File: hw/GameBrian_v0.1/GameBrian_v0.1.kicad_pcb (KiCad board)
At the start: 6 copper layers, 136.4 x 144.3 mm, 121 parts, among them J1 USB_C_Receptacle_USB2.0_16P, J2 GameBoy_GamePak_AGB-002, J3 Micro_SD_Card_Det_Hirose_DM3AT, J4 Debug, J5 Config, J6 GPIO, Q1 Q_NMOS_GSD, Q2 Q_NMOS_GSD, SW10 Program, SW8 Reset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

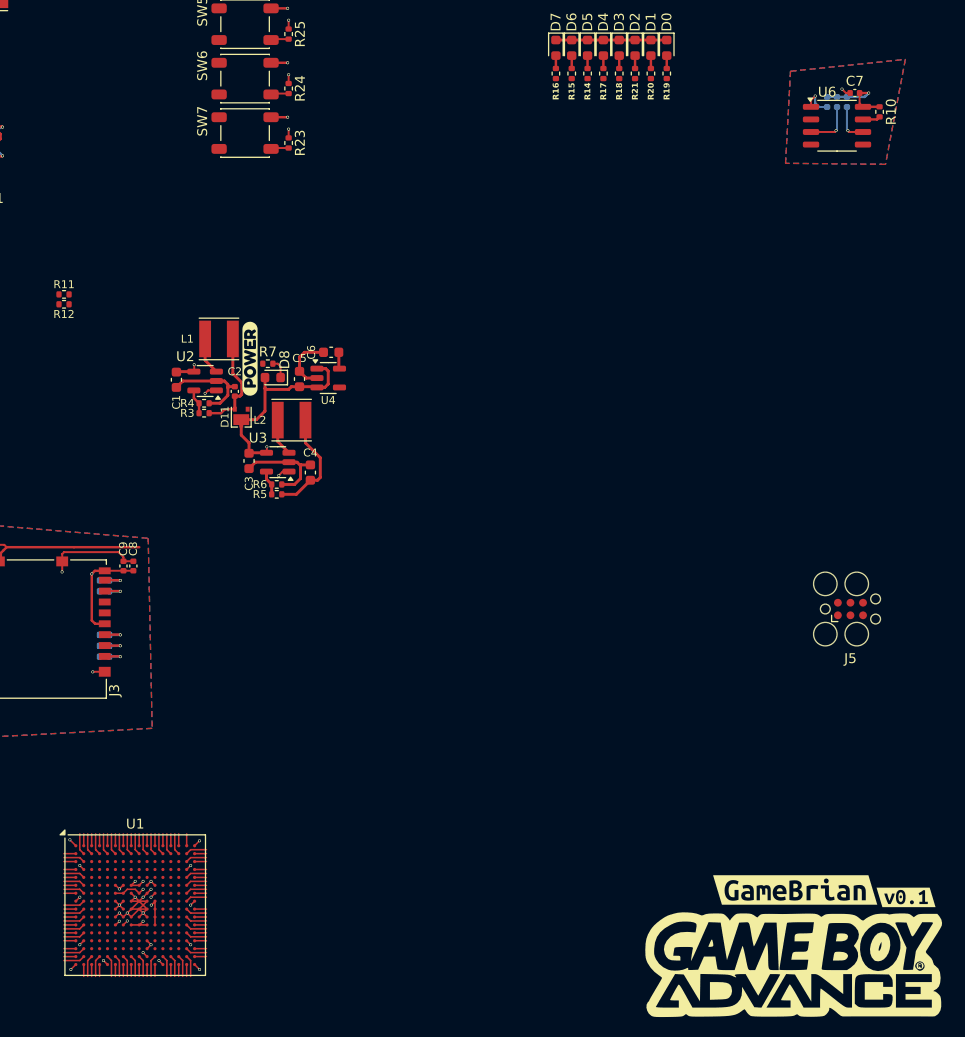
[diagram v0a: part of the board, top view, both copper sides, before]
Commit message: Checkpoint (pre-final route)
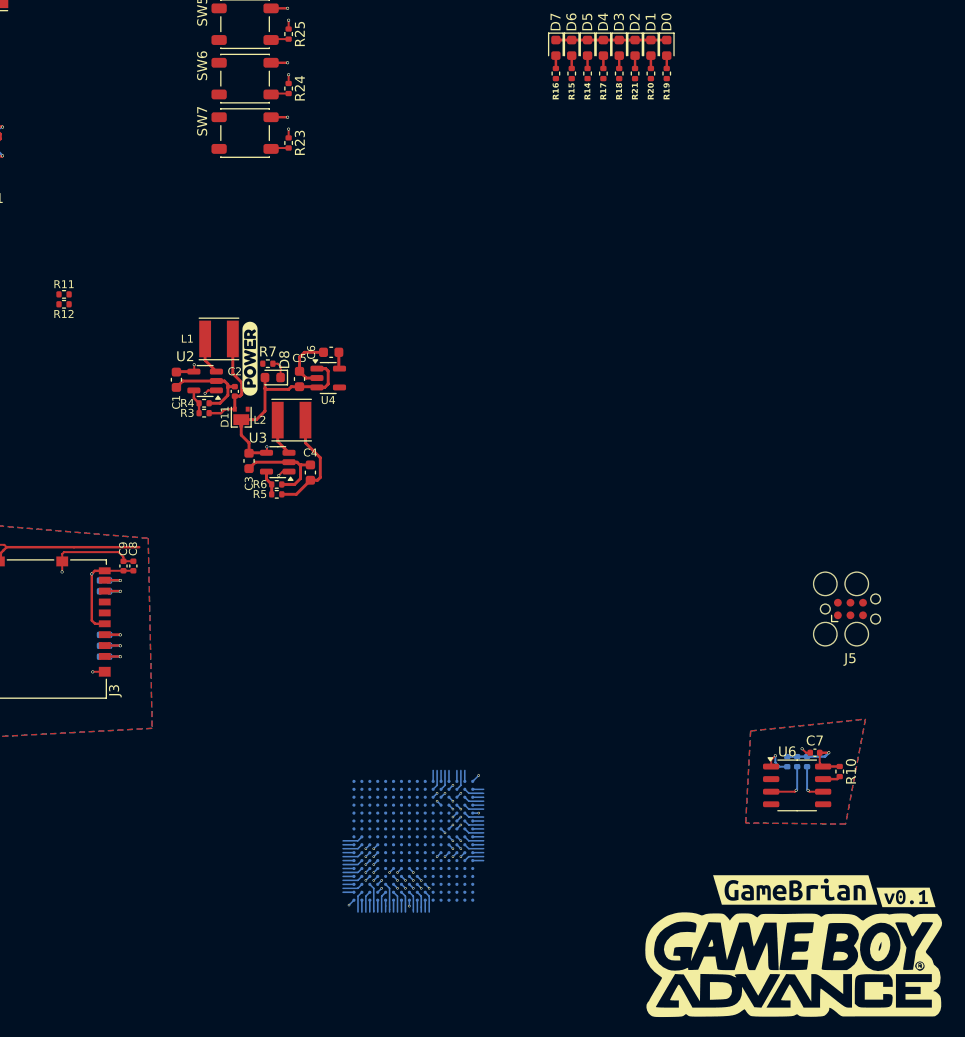
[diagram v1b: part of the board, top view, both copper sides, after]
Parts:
- U1: moved to B.Cu
- moved C7 66.8 mm to (110.6, 141.1)
- moved R10 66.8 mm to (113.1, 143.0)
- moved R38 66.8 mm to (108.8, 142.0)
- moved R39 66.8 mm to (109.8, 142.0)
- moved R40 66.8 mm to (107.8, 142.0)
- moved U6 66.8 mm to (108.8, 144.4)
- moved U1 28.8 mm to (70.0, 150.0), turned to -90 degrees
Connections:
- U1 pad N10: +3V3 -> GND
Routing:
- net GND: track 83.9 -> 62.7 mm, vias 32 -> 19
- net +3V3: track 67.6 -> 59.1 mm, vias 18 -> 13
- net (no net): track 0.00 -> 6.90 mm
- net /TDO: track 0.00 -> 5.60 mm, vias 0 -> 1
- net +1V1: track 16.5 -> 11.0 mm, vias 2 -> 0
- net unconnected-(U1D-PR20A/+/HS/RDQ17-PadG12): track 0.00 -> 4.90 mm, vias 0 -> 1
- net unconnected-(U1D-PR26A/+/HS/RDQ29-PadH12): track 0.00 -> 4.83 mm, vias 0 -> 1
- net unconnected-(U1D-PR17D/-/RDQ17-PadF12): track 0.00 -> 4.73 mm, vias 0 -> 1
- net /CFG_IO2: track 5.01 -> 9.48 mm, vias 1 -> 2
- net unconnected-(U1D-PR26B/-/HS/RDQ29-PadH13): track 0.00 -> 3.93 mm, vias 0 -> 1
- net unconnected-(U1D-PR20B/-/HS/RDQ17-PadG13): track 0.00 -> 3.93 mm, vias 0 -> 1
- net unconnected-(U1D-PR17C/+/RDQ17-PadF13): track 0.00 -> 3.93 mm, vias 0 -> 1
- net unconnected-(U1D-PR26C/+/RDQ29-PadJ13): track 0.00 -> 3.93 mm, vias 0 -> 1
- net unconnected-(U1D-PR11D/-/RDQ17-PadD14): track 0.00 -> 3.93 mm, vias 0 -> 1
- net /CFG_CLK: track 4.01 -> 7.84 mm, vias 1 -> 2
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- removed copper zone on In1.Cu, net GND
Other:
- board text added: "0"
- board text added: "1"
- board text added: "2"
- board text added: "3"
- board text added: "6"
- board text added: "7"
- board text added: "8"

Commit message: Checkpoint (DDR RAM?)
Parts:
- U1: moved to F.Cu
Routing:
- net GND: track 62.7 -> 78.3 mm, vias 19 -> 21
- net +3V3: track 59.1 -> 69.9 mm, vias 13 -> 19
- net (no net): track 6.90 -> 0.00 mm
- net +1V1: track 11.0 -> 16.8 mm, vias 0 -> 4
- net unconnected-(U1G-PL17D/-/LDQ17-PadF5): track 0.00 -> 4.96 mm, vias 0 -> 1
- net unconnected-(U1B-PT9A/+-PadE4): track 0.00 -> 4.63 mm, vias 0 -> 1
- net unconnected-(U1B-PT13A/+-PadE5): track 0.00 -> 4.63 mm, vias 0 -> 1
- net unconnected-(U1G-PL26D/-/LDQ29-PadJ5): track 0.00 -> 4.63 mm, vias 0 -> 1
- net unconnected-(U1B-PT33A/+/GR_PCLK0_1-PadE7): track 0.00 -> 4.47 mm, vias 0 -> 1
- net unconnected-(U1G-PL20B/-/HS/LDQ17-PadG4): track 0.00 -> 3.83 mm, vias 0 -> 1
- net unconnected-(U1G-PL17C/+/LDQ17-PadF4): track 0.00 -> 3.83 mm, vias 0 -> 1
- net unconnected-(U1B-PT33B/-/GR_PCLK0_0-PadD7): track 0.00 -> 3.83 mm, vias 0 -> 1
- net unconnected-(U1B-PT20B/--PadD6): track 0.00 -> 3.83 mm, vias 0 -> 1
- net unconnected-(U1G-PL26C/+/LDQ29-PadJ4): track 0.00 -> 3.83 mm, vias 0 -> 1
- net unconnected-(U1B-PT13B/--PadD5): track 0.00 -> 3.83 mm, vias 0 -> 1
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
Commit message: IDK
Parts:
- J2: footprint GameBrian:GameBoy_GamePak_AGB-002_P1.50mm_Edge_Cuts -> Connector_PinSocket_2.54mm:PinSocket_2x16_P2.54mm_Horizontal
- kibuzzard-66DEDB97: moved to B.Cu
- moved J6 287.2 mm to (344.4, 276.5)
- moved R33 257.8 mm to (213.8, 318.5)
- moved R34 257.8 mm to (213.8, 314.1)
- moved R35 257.8 mm to (213.8, 313.0)
- moved R37 257.8 mm to (213.8, 319.6)
- moved C8 257.8 mm to (216.8, 311.5)
- moved C9 257.8 mm to (215.8, 311.5)
- moved J3 257.8 mm to (206.2, 317.9)
- moved R22 257.8 mm to (202.3, 309.4)
- moved R36 257.8 mm to (213.8, 320.7)
- moved kibuzzard-66DEDB97 133.7 mm to (136.5, 118.9), turned to 90 degrees
- moved U5 122.4 mm to (118.8, 146.4)
- moved SW0 113.2 mm to (159.3, 78.8)
- moved SW1 113.2 mm to (159.3, 84.3)
- moved SW2 113.2 mm to (159.3, 89.8)
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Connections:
- U1 pad B15: unconnected-(U1D-PR11B/-/URC_GPLL0C_IN/HS/RDQ17-PadB15) -> /GBA_nREQ
- U1 pad B16: unconnected-(U1D-PR11A/+/URC_GPLL0T_IN/HS/RDQ17-PadB16) -> /GBA_nCS2
- U1 pad C14: unconnected-(U1D-PR11C/+/RDQ17-PadC14) -> /GBA_D5
- U1 pad C15: unconnected-(U1D-PR14B/-/HS/RDQ17-PadC15) -> /GBA_D7
- U1 pad C16: unconnected-(U1D-PR14A/+/HS/RDQ17-PadC16) -> /GBA_D6
- U1 pad D14: unconnected-(U1D-PR11D/-/RDQ17-PadD14) -> /GBA_D3
- U1 pad D16: unconnected-(U1D-PR17A/+/HS/RDQS17-PadD16) -> /GBA_D4
- U1 pad E14: unconnected-(U1D-PR14C/+/RDQ17-PadE14) -> /GBA_A15
- U1 pad E15: unconnected-(U1D-PR17B/-/HS/RDQSN17-PadE15) -> /GBA_D2
- U1 pad E16: unconnected-(U1D-PR20D/-/RDQ17-PadE16) -> /GBA_D1
- U1 pad F12: unconnected-(U1D-PR17D/-/RDQ17-PadF12) -> /GBA_D0
- U1 pad F13: unconnected-(U1D-PR17C/+/RDQ17-PadF13) -> /GBA_A12
- U1 pad F14: unconnected-(U1D-PR14D/-/RDQ17-PadF14) -> /GBA_A10
- U1 pad F15: unconnected-(U1D-PR20C/+/RDQ17-PadF15) -> /GBA_A11
- U1 pad F16: unconnected-(U1D-PR23A/+/HS/RDQ29-PadF16) -> /GBA_A13
- U1 pad G12: unconnected-(U1D-PR20A/+/HS/RDQ17-PadG12) -> /GBA_A14
- U1 pad G13: unconnected-(U1D-PR20B/-/HS/RDQ17-PadG13) -> /GBA_A8
- U1 pad G14: unconnected-(U1D-PR23C/+/VREF1_2/RDQ29-PadG14) -> /GBA_A6
- U1 pad G15: unconnected-(U1D-PR23B/-/HS/RDQ29-PadG15) -> /GBA_A7
- U1 pad G16: unconnected-(U1D-PR29A/+/GR_PCLK2_1/HS/RDQS29-PadG16) -> /GBA_A9
- U1 pad H12: unconnected-(U1D-PR26A/+/HS/RDQ29-PadH12) -> /GBA_A2
- U1 pad H13: unconnected-(U1D-PR26B/-/HS/RDQ29-PadH13) -> /GBA_A1
- U1 pad H14: unconnected-(U1D-PR23D/-/RDQ29-PadH14) -> /GBA_A4
- U1 pad H15: unconnected-(U1D-PR29B/-/HS/RDQSN29-PadH15) -> /GBA_A5
- U1 pad J13: unconnected-(U1D-PR26C/+/RDQ29-PadJ13) -> /GBA_nWR
- U1 pad J14: unconnected-(U1D-PR29C/+/GR_PCLK2_0/RDQ29-PadJ14) -> /GBA_nCS
- U1 pad J15: unconnected-(U1D-PR32B/-/PCLKC2_1/HS/RDQ29-PadJ15) -> /GBA_A0
- U1 pad J16: unconnected-(U1D-PR32A/+/PCLKT2_1/HS/RDQ29-PadJ16) -> /GBA_A3
- U1 pad K14: unconnected-(U1D-PR29D/-/RDQ29-PadK14) -> /GBA_VDD
- U1 pad K15: unconnected-(U1D-PR32D/-/PCLKC2_0/RDQ29-PadK15) -> /GBA_CLK
- U1 pad K16: unconnected-(U1D-PR32C/+/PCLKT2_0/RDQ29-PadK16) -> /GBA_nRD
- U1 pad N8: unconnected-(U1H-PB15A/+/HOLDN/DI/BUSY/CSSPIN/CEN-PadN8) -> /MODE_0
- U1 pad P7: unconnected-(U1H-PB6B/-/D4/MOSI2/IO4-PadP7) -> /USB_PU
- U1 pad P8: unconnected-(U1H-PB13B/-/CS1N-PadP8) -> /MODE_1
- U1 pad R6: unconnected-(U1H-PB4B/-/D6/IO6-PadR6) -> /USB_DN
- U1 pad R7: unconnected-(U1H-PB6A/+/D5/MISO2/IO5-PadR7) -> /USB_DP
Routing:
- net /DFU: track 2.96 -> 64.1 mm, vias 0 -> 2
- net /GBA_A8: track 0.00 -> 31.0 mm, vias 0 -> 1
- net /CFG_INIT: track 1.10 -> 30.8 mm, vias 0 -> 2
- net /MODE_1: track 0.00 -> 29.0 mm, vias 0 -> 2
- net /GBA_A11: track 0.00 -> 28.9 mm
- net /CFG_PROG: track 2.07 -> 30.6 mm
- net /GBA_A2: track 0.00 -> 28.5 mm, vias 0 -> 1
- net /GBA_A6: track 0.00 -> 28.3 mm, vias 0 -> 1
- net /GBA_A4: track 0.00 -> 27.6 mm, vias 0 -> 1
- net /GBA_A0: track 0.00 -> 26.1 mm
- net /GBA_A7: track 0.00 -> 26.0 mm
- net /GBA_A9: track 0.00 -> 25.9 mm
- net /MODE_0: track 0.00 -> 25.5 mm, vias 0 -> 2
- net /GBA_CLK: track 0.00 -> 25.5 mm
- net /GBA_A1: track 0.00 -> 25.1 mm, vias 0 -> 1
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- added copper zone on In1.Cu, net GND
- added copper zone on In2.Cu, net GND
- added copper zone on In3.Cu, net GND
- added copper zone on In4.Cu, net GND
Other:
- board size 136.4 x 144.3 mm -> 50.5 x 66.4 mm
